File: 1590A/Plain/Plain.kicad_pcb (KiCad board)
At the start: 2 copper layers, 32 x 86 mm, 30 parts, among them J101 Conn_01x04_Pin, J102 Barrel_Jack_Switch, J103 Conn_01x04_Pin, J104 AudioJack2_Ground, J105 AudioJack2_Ground, Q101 PMV250, Q102 BC847C, Q201 MMBF5103, Q202 BC857C

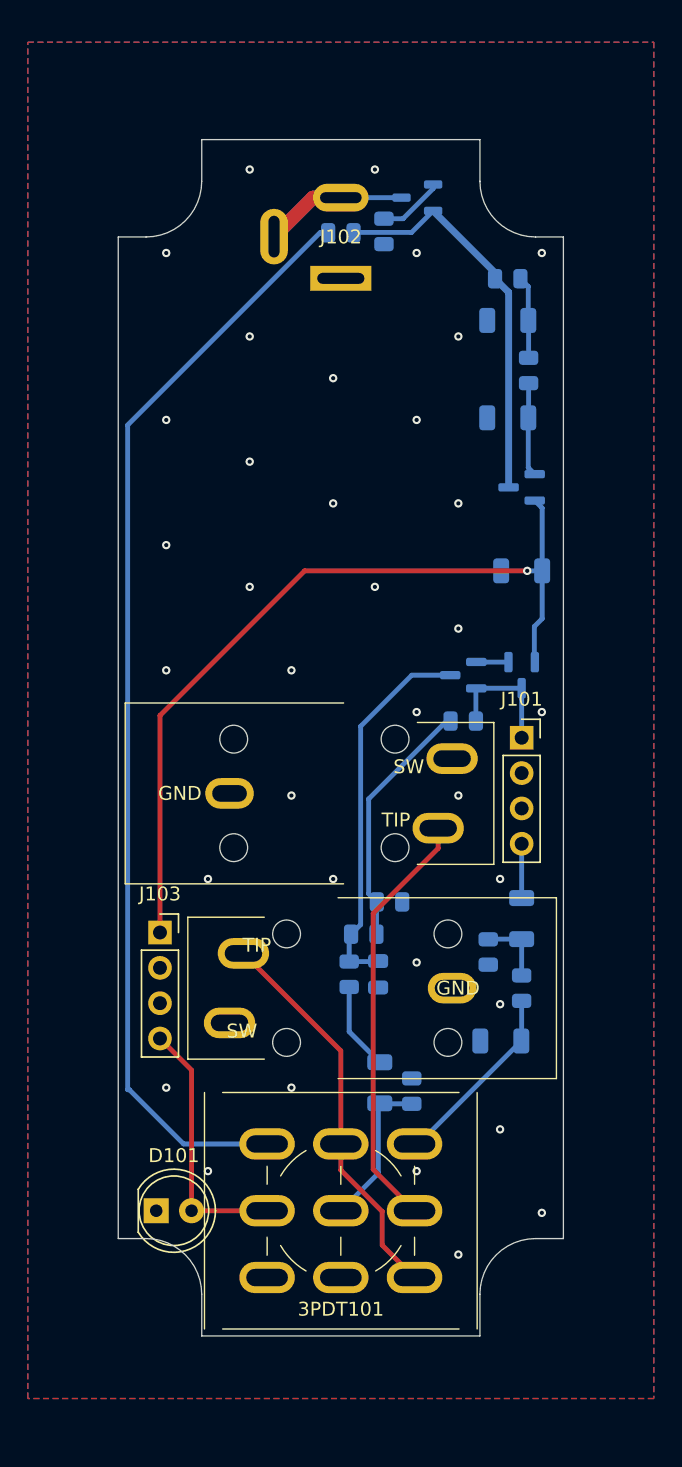
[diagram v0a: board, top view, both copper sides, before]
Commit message: Update plain 1590A board
I had decided that the effect board didn't need the input to be
ground-biased, and that was very wrong, and made some of my old effect
boards not work.  So add the AC couple capacitor and resistor to ground.

Also do the same boring RC power smoothing with the voodoo ferrite for
the +VA line.  Let's keep it simple and realistic - the noise isn't some
60Hz ripple, it's all SMPS high-frequency stuff.

Signed-off-by: Linus Torvalds <torvalds@linux-foundation.org>
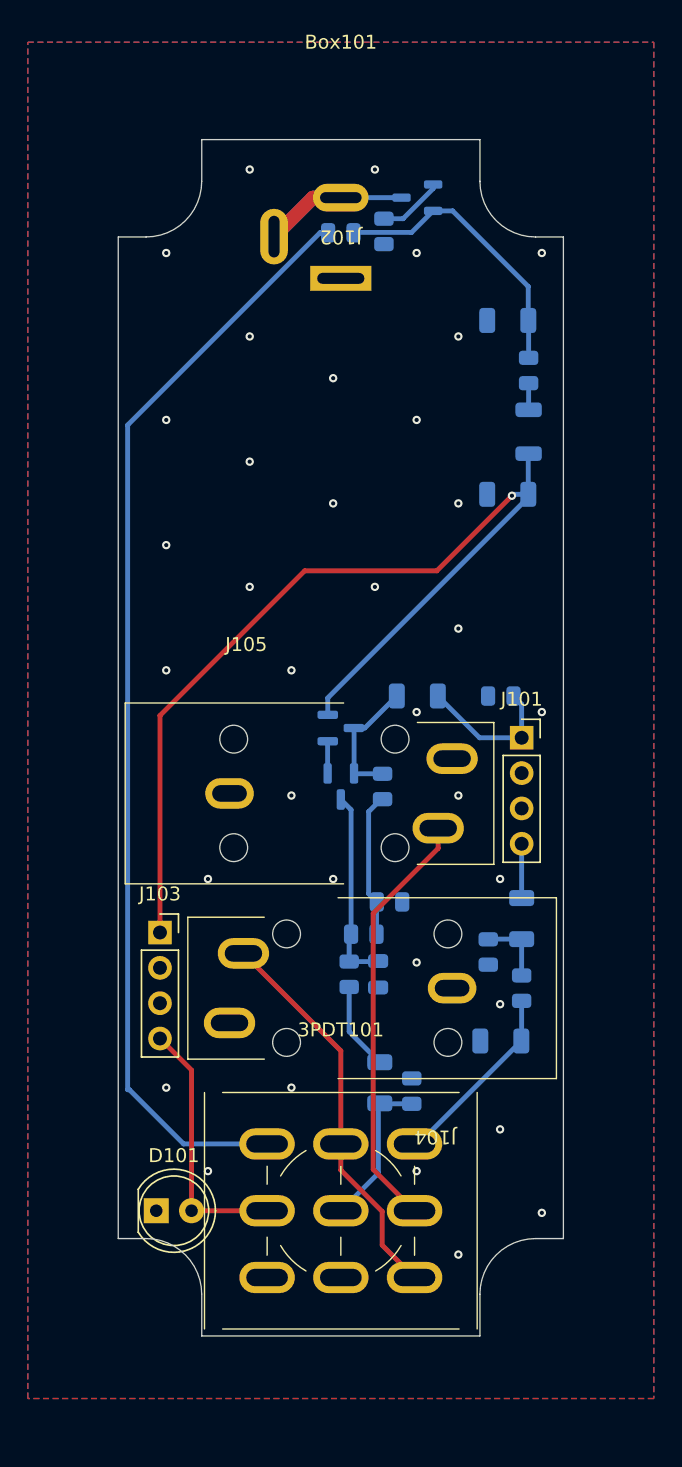
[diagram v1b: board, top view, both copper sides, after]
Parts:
- removed C102: 10uF, Capacitor_SMD:C_1206_3216Metric
- removed Q102: BC847C, Package_TO_SOT_SMD:SOT-23
- removed R103: 3k3, Resistor_SMD:R_0805_2012Metric
- added C205: 1uF, Capacitor_SMD:C_1206_3216Metric, B.Cu at (105.5, 97.0)
- added FB101: FerriteBead, Inductor_SMD:L_1206_3216Metric, B.Cu at (113.5, 78.0)
- added R208: 1MEG, Resistor_SMD:R_0805_2012Metric, B.Cu at (111.5, 97.0)
- C101, C103: value 10uF -> 22uF
- C203: value 4.7uF -> 1uF
- J104: value AudioJack2_Ground -> Input
- J105: value AudioJack2_Ground -> Output
- R104: value 3k3 -> 100R
- R204, R205: value 1k -> 2k2
- moved Q202 13.5 mm to (100.0, 99.3), turned to 0 degrees
- moved Q201 11.9 mm to (100.0, 103.5), turned to -90 degrees
- moved R204 7.47 mm to (103.0, 103.5), turned to -90 degrees
- moved C103 5.59 mm to (112.0, 82.5)
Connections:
- C101 pad 1: Net-(C101-Pad1) -> VIN
- J105 pad S: unconnected-(J105-PadS) -> GND
- Q201 pad 2: IN^{EFF} -> Net-(Q201-S)
- Q202 pad 3: IN^{EFF} -> Net-(Q201-S)
- R104 pad 1: Net-(C101-Pad1) -> VIN
- R204 pad 1: IN^{EFF} -> Net-(Q201-S)
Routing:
- net +VA: track 59.5 -> 73.4 mm
- net Net-(Q201-G): track 27.3 -> 14.1 mm
- net Net-(Q201-S): track 0.00 -> 9.37 mm
- net VIN: track 28.5 -> 20.6 mm
- net Net-(R203-Pad2): track 18.2 -> 10.4 mm
- net Net-(C101-Pad1): track 5.93 -> 0.00 mm
- net Net-(FB101-Pad1): track 6.74 -> 1.91 mm
- net IN^{EFF}: track 9.19 -> 10.5 mm
